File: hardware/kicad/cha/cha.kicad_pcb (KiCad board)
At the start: 4 copper layers, 173 x 134 mm, 137 parts, among them J1 AES_CHA, J2 CONF C, J3 CONF SM, J4 microSD, J5 Câble PROG-CHA, SW1 Retour menu, U1 AMS1117-3.3, U10 74AHCT1G32, U11 74LVC1G07, U12 iCE40HX4K-TQ144, U13 AS4C32M16SB-6TIN, U14 iCE40HX4K-TQ144, U15 IS61WV10248EDBLL-10TLI, U2 AP2112K-1.2, U3 74LVC16244A, U4 74LVC16244A, U5 74LVC16244A, U6 74LVC16244A, U7 74AHCT16244, U8 74AHCT16244, U9 74AHCT244, X1 25 MHz 3,3 V, X2 25 MHz 3,3 V

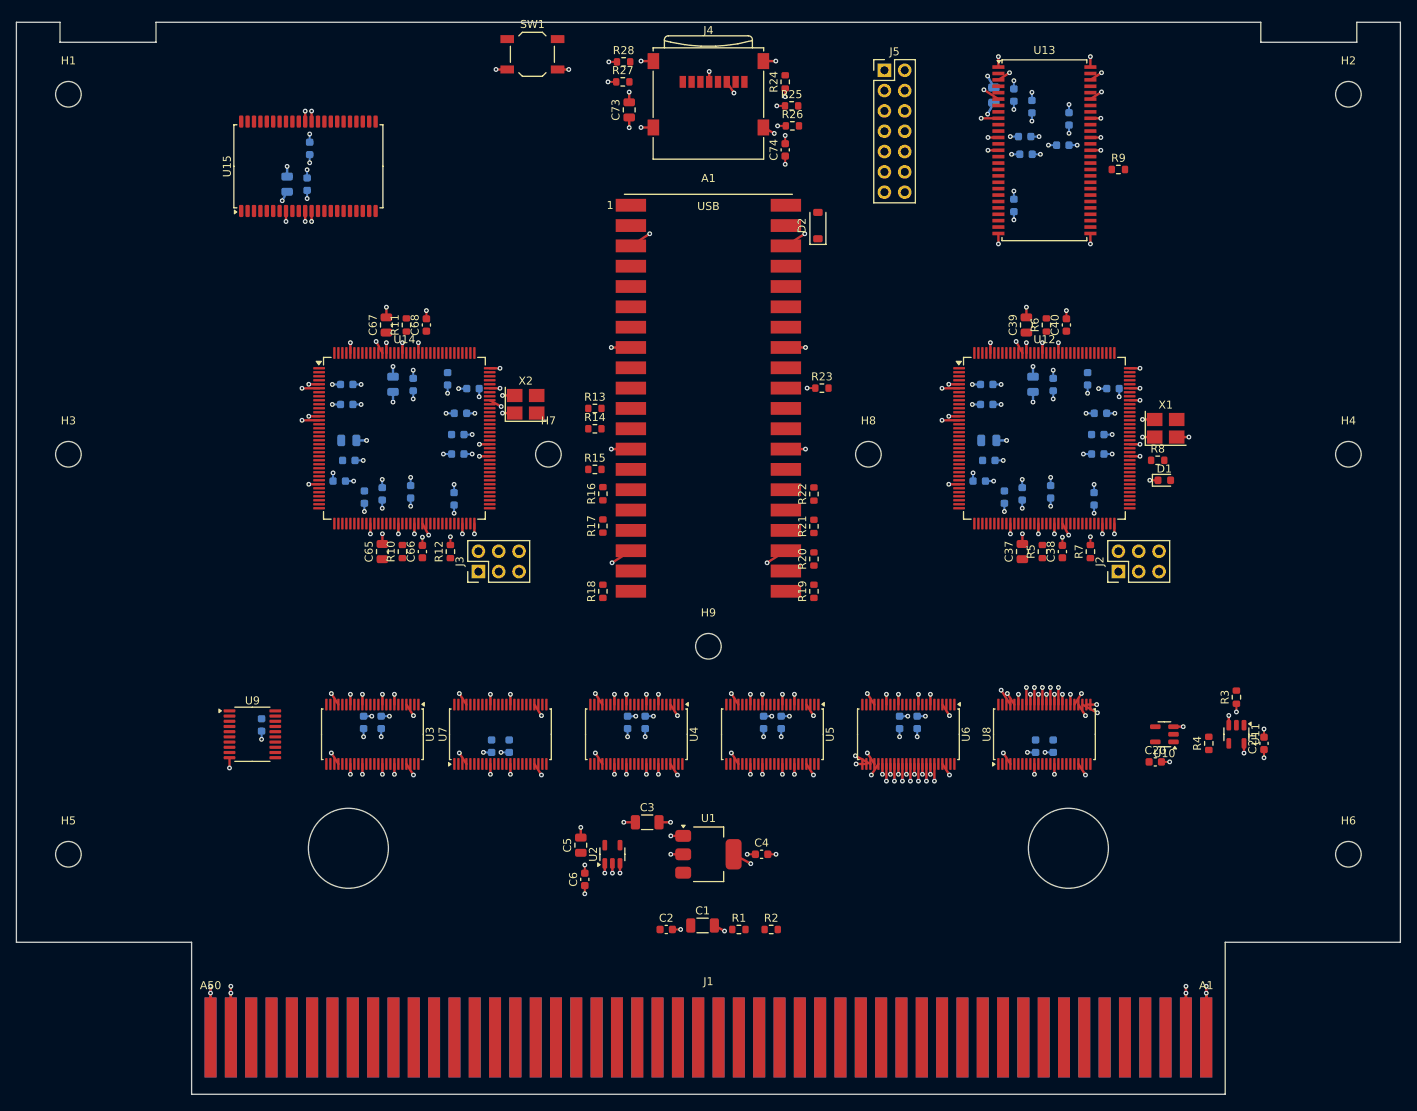
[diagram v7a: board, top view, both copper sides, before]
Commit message: PCB : vias vers les plans réglementaires et hors des couloirs de sortie
Le routage précédent (171 liaisons non routées, 40 violations dès le
départ) était faussé par les vias vers les plans : posés vers
l'extérieur des boîtiers, ils bloquaient la sortie des signaux, et leur
piste de raccordement pouvait frôler les pastilles voisines.
- direction suivant l'axe de la pastille (et non le centre du
  composant, faux près des coins et sur le connecteur de bord) ;
- QFP et SO : via sous le boîtier d'abord ; jamais sous le Pico ;
- via et piste vérifiés à 0,127 mm de tout autre réseau ;
- plans prolongés dans la languette (vias des contacts de masse).
DRC des cartes préparées : aucune violation de règle.

Co-Authored-By: Claude Opus 5.5 <noreply@anthropic.com>
Claude-Session: https://claude.ai/code/session_01WKfXP1YJ8otGxZ5dsY6Agh
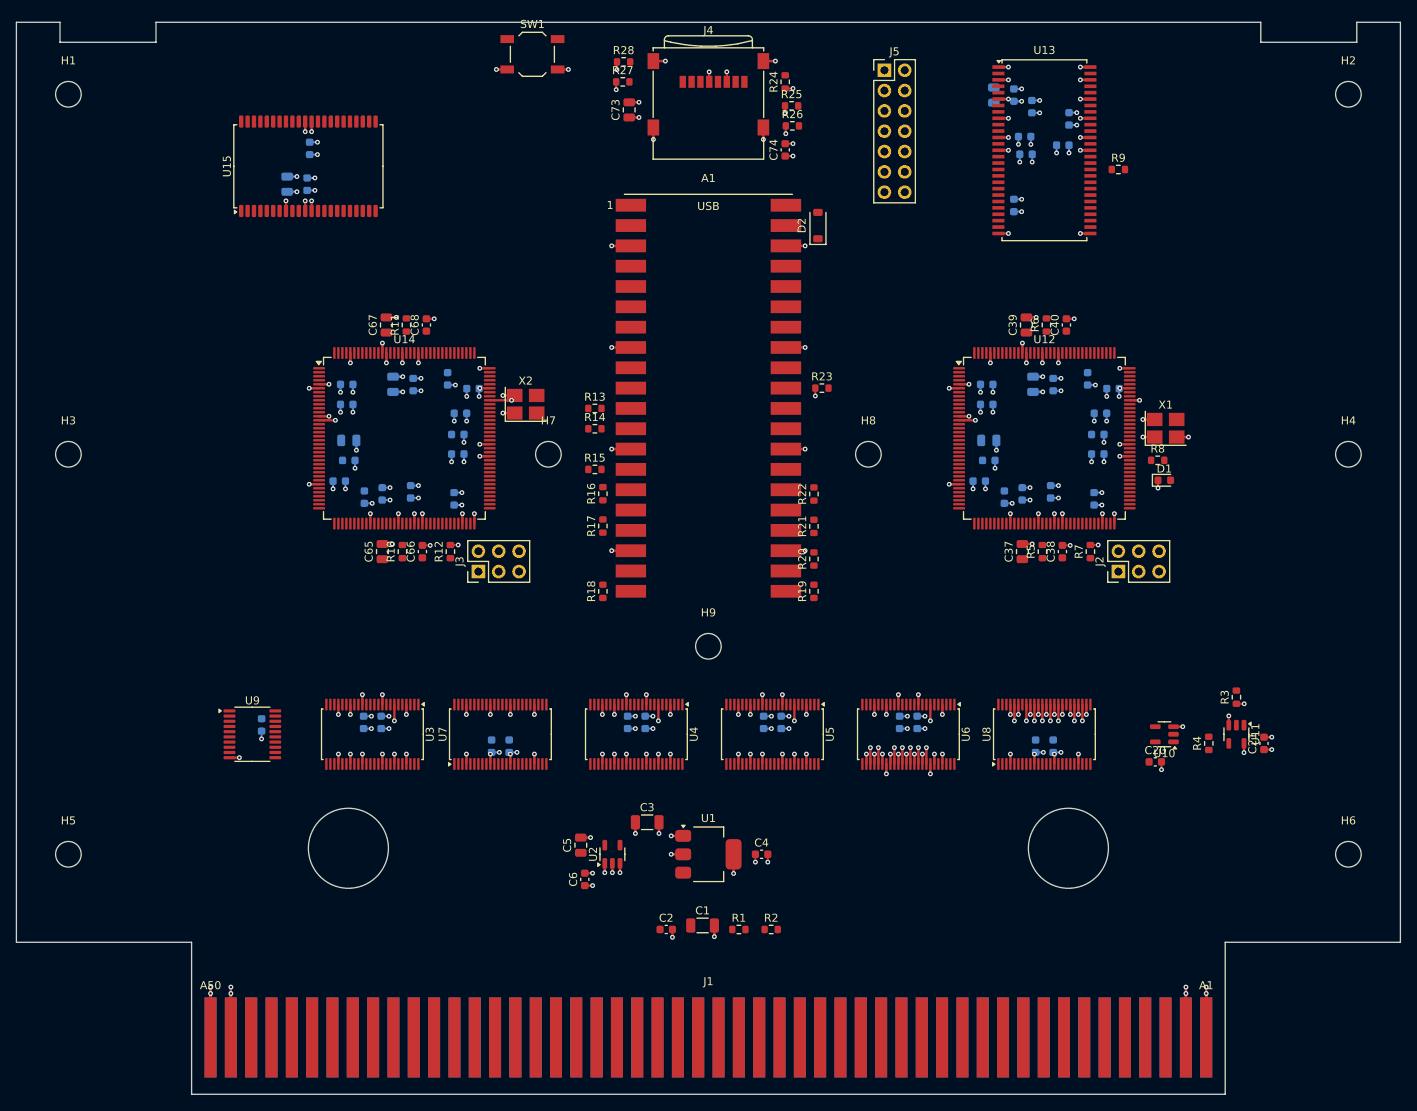
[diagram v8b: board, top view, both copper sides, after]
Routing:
- net GND: track 333.8 -> 308.0 mm, vias 213 -> 212
- net +3V3: track 135.0 -> 128.2 mm, vias 109 -> 108
